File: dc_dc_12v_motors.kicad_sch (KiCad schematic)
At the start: 18 parts

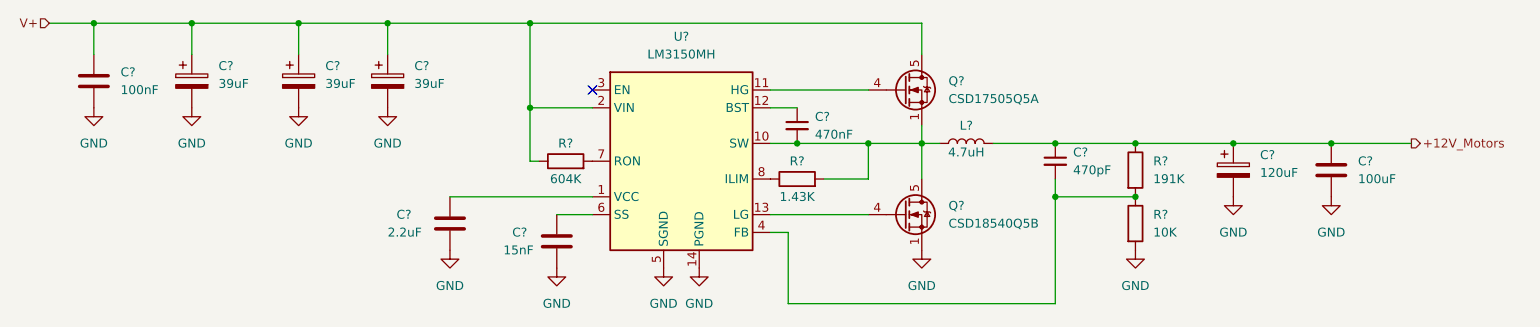
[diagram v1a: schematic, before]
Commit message: annotated all schematics, modified ext_devices
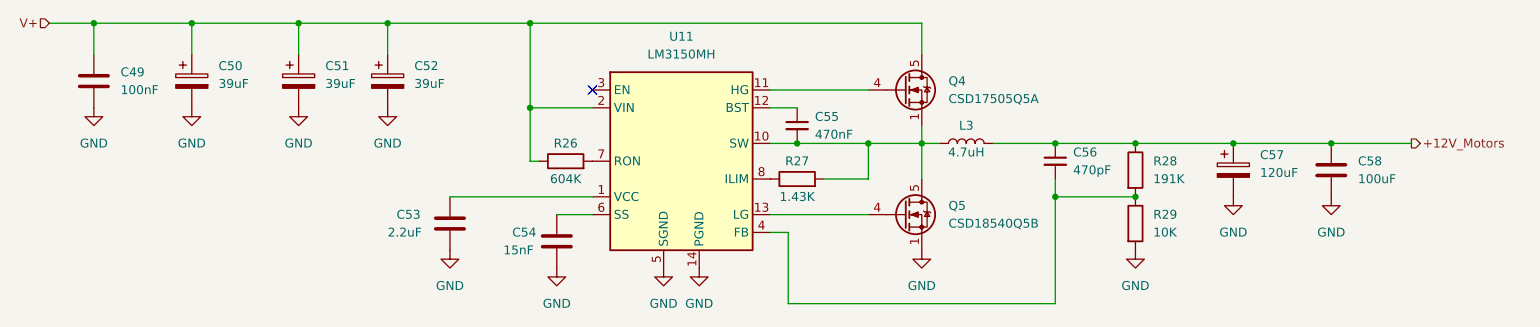
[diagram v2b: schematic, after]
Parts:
- gave numbers to parts that had none: 18
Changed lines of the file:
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@@
   (symbol (lib_id "Device:C_Polarized") (at 222.885 95.25 0) (unit 1)
     (in_bom yes) (on_board yes) (fields_autoplaced)
-    (property "Reference" "C?" (id 0) (at 226.695 93.0909 0)
+    (property "Reference" "C57" (id 0) (at 226.695 93.0909 0)
       (effects (font (size 1.27 1.27)) (justify left))
     )
@@
   (symbol (lib_id "Device:L") (at 184.785 91.44 90) (unit 1)
     (in_bom yes) (on_board yes)
-    (property "Reference" "L?" (id 0) (at 184.785 88.9 90))
+    (property "Reference" "L3" (id 0) (at 184.785 88.9 90))
     (property "Value" "4.7uH" (id 1) (at 184.785 92.71 90))
     (property "Footprint" "Robotont:IND-SMD_L17.5-W17.5" (id 2) (at 184.785 91.44 0)
@@
   (symbol (lib_id "Device:C_Small") (at 160.655 88.9 0) (unit 1)
     (in_bom yes) (on_board yes) (fields_autoplaced)
-    (property "Reference" "C?" (id 0) (at 163.195 87.6362 0)
+    (property "Reference" "C55" (id 0) (at 163.195 87.6362 0)
       (effects (font (size 1.27 1.27)) (justify left))
     )
@@
   (symbol (lib_id "Device:R") (at 160.655 96.52 90) (unit 1)
     (in_bom yes) (on_board yes)
-    (property "Reference" "R?" (id 0) (at 160.655 93.98 90))
+    (property "Reference" "R27" (id 0) (at 160.655 93.98 90))
     (property "Value" "1.43K" (id 1) (at 160.655 99.06 90))
     (property "Footprint" "Resistor_SMD:R_0805_2012Metric_Pad1.20x1.40mm_HandSolder" (id 2) (at 160.655 98.298 90)
@@
   (symbol (lib_id "Device:C") (at 111.125 102.87 0) (unit 1)
     (in_bom yes) (on_board yes)
-    (property "Reference" "C?" (id 0) (at 103.505 101.6 0)
+    (property "Reference" "C53" (id 0) (at 103.505 101.6 0)
       (effects (font (size 1.27 1.27)) (justify left))
     )
@@
   (symbol (lib_id "Device:C") (at 60.325 82.55 0) (unit 1)
     (in_bom yes) (on_board yes) (fields_autoplaced)
-    (property "Reference" "C?" (id 0) (at 64.135 81.2799 0)
+    (property "Reference" "C49" (id 0) (at 64.135 81.2799 0)
       (effects (font (size 1.27 1.27)) (justify left))
     )
@@
   (symbol (lib_id "Transistor_FET:CSD17505Q5A") (at 175.895 83.82 0) (unit 1)
     (in_bom yes) (on_board yes) (fields_autoplaced)
-    (property "Reference" "Q?" (id 0) (at 182.245 82.5499 0)
+    (property "Reference" "Q4" (id 0) (at 182.245 82.5499 0)
       (effects (font (size 1.27 1.27)) (justify left))
     )
@@
   (symbol (lib_id "Device:C") (at 236.855 95.25 0) (unit 1)
     (in_bom yes) (on_board yes) (fields_autoplaced)
-    (property "Reference" "C?" (id 0) (at 240.665 93.9799 0)
+    (property "Reference" "C58" (id 0) (at 240.665 93.9799 0)
       (effects (font (size 1.27 1.27)) (justify left))
     )
@@
   (symbol (lib_id "Device:C_Small") (at 197.485 93.98 0) (unit 1)
     (in_bom yes) (on_board yes) (fields_autoplaced)
-    (property "Reference" "C?" (id 0) (at 200.025 92.7162 0)
+    (property "Reference" "C56" (id 0) (at 200.025 92.7162 0)
       (effects (font (size 1.27 1.27)) (justify left))
     )
@@
   (symbol (lib_id "Device:R") (at 127.635 93.98 90) (unit 1)
     (in_bom yes) (on_board yes)
-    (property "Reference" "R?" (id 0) (at 127.635 91.44 90))
+    (property "Reference" "R26" (id 0) (at 127.635 91.44 90))
     (property "Value" "604K" (id 1) (at 127.635 96.52 90))
     (property "Footprint" "Resistor_SMD:R_0805_2012Metric_Pad1.20x1.40mm_HandSolder" (id 2) (at 127.635 95.758 90)
@@
   (symbol (lib_id "Device:C_Polarized") (at 74.295 82.55 0) (unit 1)
     (in_bom yes) (on_board yes) (fields_autoplaced)
-    (property "Reference" "C?" (id 0) (at 78.105 80.3909 0)
+    (property "Reference" "C50" (id 0) (at 78.105 80.3909 0)
       (effects (font (size 1.27 1.27)) (justify left))
     )
@@
   (symbol (lib_id "Device:C_Polarized") (at 102.235 82.55 0) (unit 1)
     (in_bom yes) (on_board yes) (fields_autoplaced)
-    (property "Reference" "C?" (id 0) (at 106.045 80.3909 0)
+    (property "Reference" "C52" (id 0) (at 106.045 80.3909 0)
       (effects (font (size 1.27 1.27)) (justify left))
     )
@@
   (symbol (lib_id "Device:C_Polarized") (at 89.535 82.55 0) (unit 1)
     (in_bom yes) (on_board yes) (fields_autoplaced)
-    (property "Reference" "C?" (id 0) (at 93.345 80.3909 0)
+    (property "Reference" "C51" (id 0) (at 93.345 80.3909 0)
       (effects (font (size 1.27 1.27)) (justify left))
     )
@@
   (symbol (lib_id "Device:R") (at 208.915 95.25 0) (unit 1)
     (in_bom yes) (on_board yes) (fields_autoplaced)
-    (property "Reference" "R?" (id 0) (at 211.455 93.9799 0)
+    (property "Reference" "R28" (id 0) (at 211.455 93.9799 0)
       (effects (font (size 1.27 1.27)) (justify left))
     )
@@
   (symbol (lib_id "Regulator_Switching:LM3150MH") (at 144.145 93.98 0) (unit 1)
     (in_bom yes) (on_board yes) (fields_autoplaced)
-    (property "Reference" "U?" (id 0) (at 144.145 76.2 0))
+    (property "Reference" "U11" (id 0) (at 144.145 76.2 0))
     (property "Value" "LM3150MH" (id 1) (at 144.145 78.74 0))
     (property "Footprint" "Package_SO:HTSSOP-14-1EP_4.4x5mm_P0.65mm_EP3.4x5mm_Mask3x3.1mm" (id 2) (at 146.685 107.95 0)
@@
   (symbol (lib_id "Transistor_FET:CSD18540Q5B") (at 175.895 101.6 0) (unit 1)
     (in_bom yes) (on_board yes) (fields_autoplaced)
-    (property "Reference" "Q?" (id 0) (at 182.245 100.3299 0)
+    (property "Reference" "Q5" (id 0) (at 182.245 100.3299 0)
       (effects (font (size 1.27 1.27)) (justify left))
     )
@@
   (symbol (lib_id "Device:C") (at 126.365 105.41 0) (unit 1)
     (in_bom yes) (on_board yes)
-    (property "Reference" "C?" (id 0) (at 120.015 104.14 0)
+    (property "Reference" "C54" (id 0) (at 120.015 104.14 0)
       (effects (font (size 1.27 1.27)) (justify left))
     )
@@
   (symbol (lib_id "Device:R") (at 208.915 102.87 0) (unit 1)
     (in_bom yes) (on_board yes) (fields_autoplaced)
-    (property "Reference" "R?" (id 0) (at 211.455 101.5999 0)
-      (effects (font (size 1.27 1.27)) (justify left))
-    )
+    (property "Reference" "R29" (id 0) (at 211.455 101.5999 0)
+      (effects (font (size 1.27 1.27)) (justify left))
+    )

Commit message: replaced main MCU, reannotated
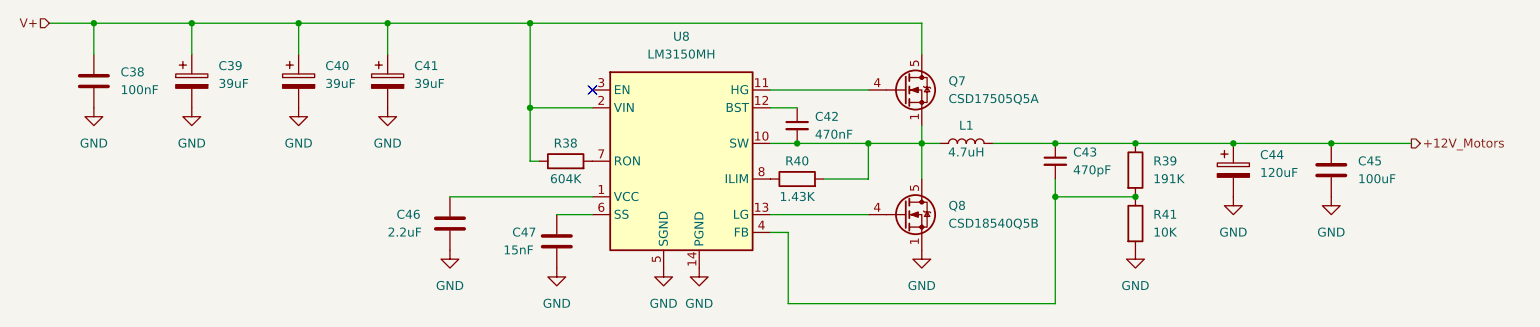
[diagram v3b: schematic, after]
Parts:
- renumbered C49 to C38, C50 to C39, C51 to C40, C52 to C41, C55 to C42, C56 to C43, C57 to C44, C58 to C45, C53 to C46, C54 to C47, L3 to L1, Q4 to Q7, Q5 to Q8, R26 to R38, R28 to R39, R27 to R40, R29 to R41, U11 to U8
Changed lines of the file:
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@@
   (symbol (lib_id "Device:C_Polarized") (at 222.885 95.25 0) (unit 1)
     (in_bom yes) (on_board yes) (fields_autoplaced)
-    (property "Reference" "C57" (id 0) (at 226.695 93.0909 0)
+    (property "Reference" "C44" (id 0) (at 226.695 93.0909 0)
       (effects (font (size 1.27 1.27)) (justify left))
     )
@@
   (symbol (lib_id "power:GND") (at 102.235 86.36 0) (unit 1)
     (in_bom yes) (on_board yes) (fields_autoplaced)
-    (property "Reference" "#PWR0167" (id 0) (at 102.235 92.71 0)
+    (property "Reference" "#PWR068" (id 0) (at 102.235 92.71 0)
       (effects (font (size 1.27 1.27)) hide)
     )
@@
   (symbol (lib_id "power:GND") (at 222.885 99.06 0) (unit 1)
     (in_bom yes) (on_board yes) (fields_autoplaced)
-    (property "Reference" "#PWR0165" (id 0) (at 222.885 105.41 0)
+    (property "Reference" "#PWR069" (id 0) (at 222.885 105.41 0)
       (effects (font (size 1.27 1.27)) hide)
     )
@@
   (symbol (lib_id "power:GND") (at 236.855 99.06 0) (unit 1)
     (in_bom yes) (on_board yes) (fields_autoplaced)
-    (property "Reference" "#PWR0164" (id 0) (at 236.855 105.41 0)
+    (property "Reference" "#PWR070" (id 0) (at 236.855 105.41 0)
       (effects (font (size 1.27 1.27)) hide)
     )
@@
   (symbol (lib_id "Device:L") (at 184.785 91.44 90) (unit 1)
     (in_bom yes) (on_board yes)
-    (property "Reference" "L3" (id 0) (at 184.785 88.9 90))
+    (property "Reference" "L1" (id 0) (at 184.785 88.9 90))
     (property "Value" "4.7uH" (id 1) (at 184.785 92.71 90))
     (property "Footprint" "Robotont:IND-SMD_L17.5-W17.5" (id 2) (at 184.785 91.44 0)
@@
   (symbol (lib_id "Device:C_Small") (at 160.655 88.9 0) (unit 1)
     (in_bom yes) (on_board yes) (fields_autoplaced)
-    (property "Reference" "C55" (id 0) (at 163.195 87.6362 0)
+    (property "Reference" "C42" (id 0) (at 163.195 87.6362 0)
       (effects (font (size 1.27 1.27)) (justify left))
     )
@@
   (symbol (lib_id "Device:R") (at 160.655 96.52 90) (unit 1)
     (in_bom yes) (on_board yes)
-    (property "Reference" "R27" (id 0) (at 160.655 93.98 90))
+    (property "Reference" "R40" (id 0) (at 160.655 93.98 90))
     (property "Value" "1.43K" (id 1) (at 160.655 99.06 90))
     (property "Footprint" "Resistor_SMD:R_0805_2012Metric_Pad1.20x1.40mm_HandSolder" (id 2) (at 160.655 98.298 90)
@@
   (symbol (lib_id "power:GND") (at 208.915 106.68 0) (unit 1)
     (in_bom yes) (on_board yes) (fields_autoplaced)
-    (property "Reference" "#PWR0162" (id 0) (at 208.915 113.03 0)
+    (property "Reference" "#PWR073" (id 0) (at 208.915 113.03 0)
       (effects (font (size 1.27 1.27)) hide)
     )
@@
   (symbol (lib_id "power:GND") (at 146.685 109.22 0) (unit 1)
     (in_bom yes) (on_board yes) (fields_autoplaced)
-    (property "Reference" "#PWR0158" (id 0) (at 146.685 115.57 0)
+    (property "Reference" "#PWR076" (id 0) (at 146.685 115.57 0)
       (effects (font (size 1.27 1.27)) hide)
     )
@@
   (symbol (lib_id "Device:C") (at 111.125 102.87 0) (unit 1)
     (in_bom yes) (on_board yes)
-    (property "Reference" "C53" (id 0) (at 103.505 101.6 0)
+    (property "Reference" "C46" (id 0) (at 103.505 101.6 0)
       (effects (font (size 1.27 1.27)) (justify left))
     )
@@
   (symbol (lib_id "power:GND") (at 74.295 86.36 0) (unit 1)
     (in_bom yes) (on_board yes) (fields_autoplaced)
-    (property "Reference" "#PWR0169" (id 0) (at 74.295 92.71 0)
+    (property "Reference" "#PWR066" (id 0) (at 74.295 92.71 0)
       (effects (font (size 1.27 1.27)) hide)
     )
@@
   (symbol (lib_id "Device:C") (at 60.325 82.55 0) (unit 1)
     (in_bom yes) (on_board yes) (fields_autoplaced)
-    (property "Reference" "C49" (id 0) (at 64.135 81.2799 0)
+    (property "Reference" "C38" (id 0) (at 64.135 81.2799 0)
       (effects (font (size 1.27 1.27)) (justify left))
     )
@@
   (symbol (lib_id "power:GND") (at 126.365 109.22 0) (unit 1)
     (in_bom yes) (on_board yes) (fields_autoplaced)
-    (property "Reference" "#PWR0160" (id 0) (at 126.365 115.57 0)
+    (property "Reference" "#PWR074" (id 0) (at 126.365 115.57 0)
       (effects (font (size 1.27 1.27)) hide)
     )
@@
   (symbol (lib_id "power:GND") (at 89.535 86.36 0) (unit 1)
     (in_bom yes) (on_board yes) (fields_autoplaced)
-    (property "Reference" "#PWR0166" (id 0) (at 89.535 92.71 0)
+    (property "Reference" "#PWR067" (id 0) (at 89.535 92.71 0)
       (effects (font (size 1.27 1.27)) hide)
     )
@@
   (symbol (lib_id "Transistor_FET:CSD17505Q5A") (at 175.895 83.82 0) (unit 1)
     (in_bom yes) (on_board yes) (fields_autoplaced)
-    (property "Reference" "Q4" (id 0) (at 182.245 82.5499 0)
+    (property "Reference" "Q7" (id 0) (at 182.245 82.5499 0)
       (effects (font (size 1.27 1.27)) (justify left))
     )
@@
   (symbol (lib_id "Device:C") (at 236.855 95.25 0) (unit 1)
     (in_bom yes) (on_board yes) (fields_autoplaced)
-    (property "Reference" "C58" (id 0) (at 240.665 93.9799 0)
+    (property "Reference" "C45" (id 0) (at 240.665 93.9799 0)
       (effects (font (size 1.27 1.27)) (justify left))
     )
@@
   (symbol (lib_id "Device:C_Small") (at 197.485 93.98 0) (unit 1)
     (in_bom yes) (on_board yes) (fields_autoplaced)
-    (property "Reference" "C56" (id 0) (at 200.025 92.7162 0)
+    (property "Reference" "C43" (id 0) (at 200.025 92.7162 0)
       (effects (font (size 1.27 1.27)) (justify left))
     )
@@
   (symbol (lib_id "Device:R") (at 127.635 93.98 90) (unit 1)
     (in_bom yes) (on_board yes)
-    (property "Reference" "R26" (id 0) (at 127.635 91.44 90))
+    (property "Reference" "R38" (id 0) (at 127.635 91.44 90))
     (property "Value" "604K" (id 1) (at 127.635 96.52 90))
     (property "Footprint" "Resistor_SMD:R_0805_2012Metric_Pad1.20x1.40mm_HandSolder" (id 2) (at 127.635 95.758 90)
@@
   (symbol (lib_id "Device:C_Polarized") (at 74.295 82.55 0) (unit 1)
     (in_bom yes) (on_board yes) (fields_autoplaced)
-    (property "Reference" "C50" (id 0) (at 78.105 80.3909 0)
+    (property "Reference" "C39" (id 0) (at 78.105 80.3909 0)
       (effects (font (size 1.27 1.27)) (justify left))
     )
@@
   (symbol (lib_id "Device:C_Polarized") (at 102.235 82.55 0) (unit 1)
     (in_bom yes) (on_board yes) (fields_autoplaced)
-    (property "Reference" "C52" (id 0) (at 106.045 80.3909 0)
+    (property "Reference" "C41" (id 0) (at 106.045 80.3909 0)
       (effects (font (size 1.27 1.27)) (justify left))
     )
@@
   (symbol (lib_id "Device:C_Polarized") (at 89.535 82.55 0) (unit 1)
     (in_bom yes) (on_board yes) (fields_autoplaced)
-    (property "Reference" "C51" (id 0) (at 93.345 80.3909 0)
+    (property "Reference" "C40" (id 0) (at 93.345 80.3909 0)
       (effects (font (size 1.27 1.27)) (justify left))
     )
@@
   (symbol (lib_id "Device:R") (at 208.915 95.25 0) (unit 1)
     (in_bom yes) (on_board yes) (fields_autoplaced)
-    (property "Reference" "R28" (id 0) (at 211.455 93.9799 0)
+    (property "Reference" "R39" (id 0) (at 211.455 93.9799 0)
       (effects (font (size 1.27 1.27)) (justify left))
     )
@@
   (symbol (lib_id "Regulator_Switching:LM3150MH") (at 144.145 93.98 0) (unit 1)
     (in_bom yes) (on_board yes) (fields_autoplaced)
-    (property "Reference" "U11" (id 0) (at 144.145 76.2 0))
+    (property "Reference" "U8" (id 0) (at 144.145 76.2 0))
     (property "Value" "LM3150MH" (id 1) (at 144.145 78.74 0))
     (property "Footprint" "Package_SO:HTSSOP-14-1EP_4.4x5mm_P0.65mm_EP3.4x5mm_Mask3x3.1mm" (id 2) (at 146.685 107.95 0)
@@
   (symbol (lib_id "power:GND") (at 141.605 109.22 0) (unit 1)
     (in_bom yes) (on_board yes) (fields_autoplaced)
-    (property "Reference" "#PWR0159" (id 0) (at 141.605 115.57 0)
+    (property "Reference" "#PWR075" (id 0) (at 141.605 115.57 0)
       (effects (font (size 1.27 1.27)) hide)
     )
@@
   (symbol (lib_id "Transistor_FET:CSD18540Q5B") (at 175.895 101.6 0) (unit 1)
     (in_bom yes) (on_board yes) (fields_autoplaced)
-    (property "Reference" "Q5" (id 0) (at 182.245 100.3299 0)
+    (property "Reference" "Q8" (id 0) (at 182.245 100.3299 0)
       (effects (font (size 1.27 1.27)) (justify left))
     )
@@
   (symbol (lib_id "power:GND") (at 111.125 106.68 0) (unit 1)
     (in_bom yes) (on_board yes) (fields_autoplaced)
-    (property "Reference" "#PWR0161" (id 0) (at 111.125 113.03 0)
+    (property "Reference" "#PWR071" (id 0) (at 111.125 113.03 0)
       (effects (font (size 1.27 1.27)) hide)
     )
@@
   (symbol (lib_id "power:GND") (at 60.325 86.36 0) (unit 1)
     (in_bom yes) (on_board yes) (fields_autoplaced)
-    (property "Reference" "#PWR0168" (id 0) (at 60.325 92.71 0)
+    (property "Reference" "#PWR065" (id 0) (at 60.325 92.71 0)
       (effects (font (size 1.27 1.27)) hide)
     )
@@
   (symbol (lib_id "power:GND") (at 178.435 106.68 0) (unit 1)
     (in_bom yes) (on_board yes) (fields_autoplaced)
-    (property "Reference" "#PWR0163" (id 0) (at 178.435 113.03 0)
+    (property "Reference" "#PWR072" (id 0) (at 178.435 113.03 0)
       (effects (font (size 1.27 1.27)) hide)
     )
@@
   (symbol (lib_id "Device:C") (at 126.365 105.41 0) (unit 1)
     (in_bom yes) (on_board yes)
-    (property "Reference" "C54" (id 0) (at 120.015 104.14 0)
+    (property "Reference" "C47" (id 0) (at 120.015 104.14 0)
       (effects (font (size 1.27 1.27)) (justify left))
     )
@@
   (symbol (lib_id "Device:R") (at 208.915 102.87 0) (unit 1)
     (in_bom yes) (on_board yes) (fields_autoplaced)
-    (property "Reference" "R29" (id 0) (at 211.455 101.5999 0)
-      (effects (font (size 1.27 1.27)) (justify left))
-    )
+    (property "Reference" "R41" (id 0) (at 211.455 101.5999 0)
+      (effects (font (size 1.27 1.27)) (justify left))
+    )
